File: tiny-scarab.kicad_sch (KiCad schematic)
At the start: 40 parts, among them J2 TC2050-IDC-NL, J3 CONN_PIN_HEADER_02x07, J4 CONN_PIN_HEADER_02x07, J5 3mm, J6 3mm, J7 3mm, J8 3mm

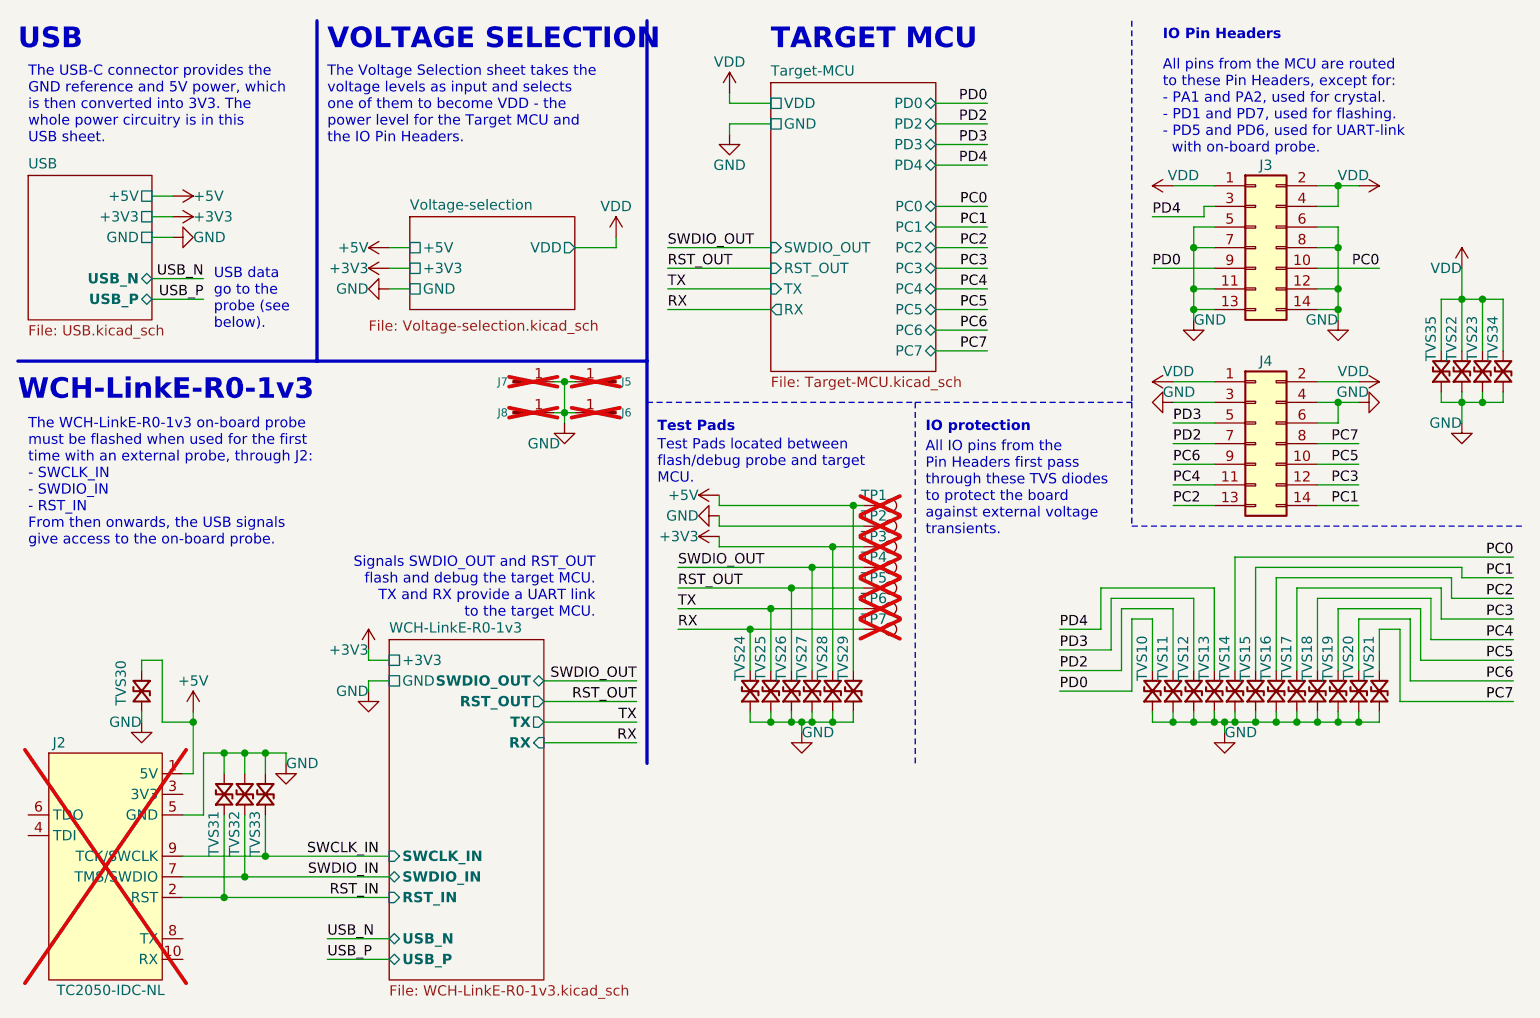
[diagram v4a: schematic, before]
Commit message: Rename net 'RST_OUT' into 'RST_CH32V003'
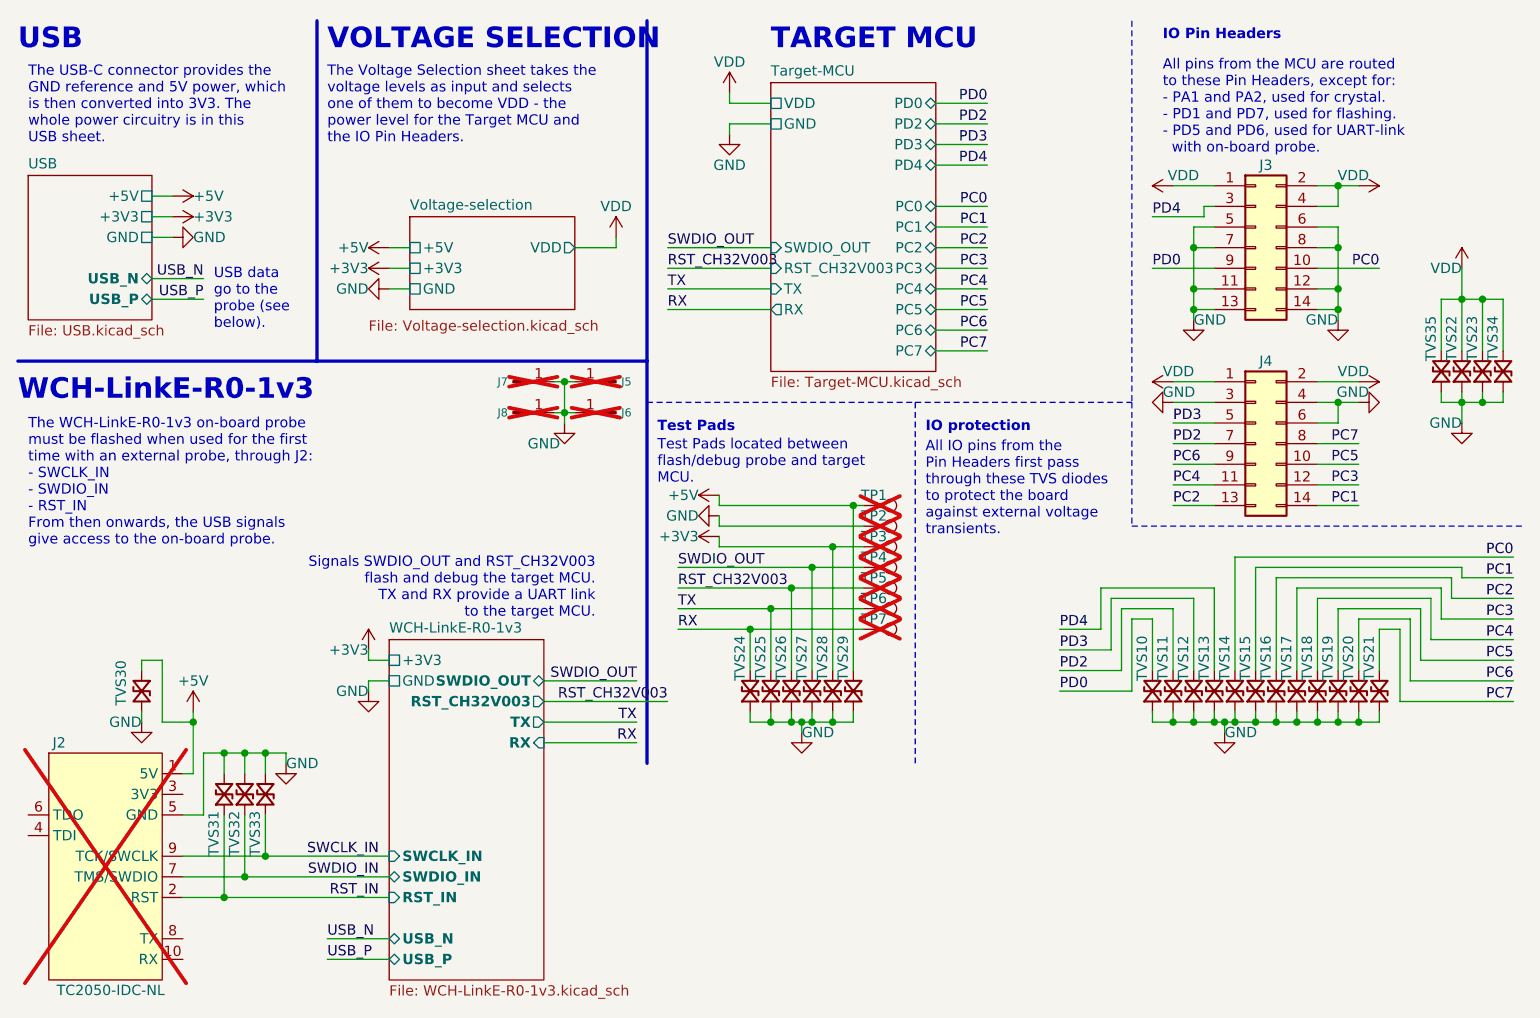
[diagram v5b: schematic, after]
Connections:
- net RST_OUT renamed RST_CH32V003
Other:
- sheet Target-MCU ports: added RST_CH32V003; removed RST_OUT
- sheet WCH-LinkE-R0-1v3 ports: added RST_CH32V003; removed RST_OUT
- note added: "Signals SWDIO_OUT and RST_CH32V003 flash and debug the target MCU. TX and RX provide a UART link to the target MCU."
- note removed: "Signals SWDIO_OUT and RST_OUT flash and debug the target MCU. TX and RX provide a UART link to the target MCU."
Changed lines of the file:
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@@
     (stroke (width 0) (type default))
   )
-  (wire (pts (xy 77.47 96.52) (xy 88.9 96.52))
+  (wire (pts (xy 77.47 96.52) (xy 92.71 96.52))
     (stroke (width 0) (type default))
   )
@@
     (effects (font (size 2.54 2.54) (thickness 0.508) bold) (justify left bottom))
   )
-  (text "Signals SWDIO_OUT and RST_OUT\nflash and debug the target MCU.\nTX and RX provide a UART link\nto the target MCU."
+  (text "Signals SWDIO_OUT and RST_CH32V003\nflash and debug the target MCU.\nTX and RX provide a UART link\nto the target MCU."
     (at 83.82 86.36 0)
     (effects (font (size 1.27 1.27)) (justify right bottom))
@@
     (effects (font (size 1.27 1.27)) (justify right bottom))
   )
-  (label "RST_OUT" (at 93.98 82.55 0) (fields_autoplaced)
+  (label "RST_CH32V003" (at 93.98 82.55 0) (fields_autoplaced)
     (effects (font (size 1.27 1.27)) (justify left bottom))
   )
@@
     (effects (font (size 1.27 1.27)) (justify left bottom))
   )
-  (label "RST_OUT" (at 92.71 43.18 0) (fields_autoplaced)
+  (label "RST_CH32V003" (at 92.71 43.18 0) (fields_autoplaced)
     (effects (font (size 1.27 1.27)) (justify left bottom))
   )
@@
     (effects (font (size 1.27 1.27)) (justify right bottom))
   )
-  (label "RST_OUT" (at 88.9 96.52 180) (fields_autoplaced)
+  (label "RST_CH32V003" (at 92.71 96.52 180) (fields_autoplaced)
     (effects (font (size 1.27 1.27)) (justify right bottom))
   )
@@
       (effects (font (size 1.27 1.27) (thickness 0.254) bold) (justify right))
     )
-    (pin "RST_OUT" output (at 77.47 96.52 0)
+    (pin "RST_CH32V003" output (at 77.47 96.52 0)
       (effects (font (size 1.27 1.27) (thickness 0.254) bold) (justify right))
     )
@@
       (effects (font (size 1.27 1.27)) (justify left))
     )
-    (pin "RST_OUT" input (at 105.41 43.18 180)
-      (effects (font (size 1.27 1.27)) (justify left))
-    )
+    (pin "RST_CH32V003" input (at 105.41 43.18 180)
+      (effects (font (size 1.27 1.27)) (justify left))
+    )

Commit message: Rename net 'RST_IN' into 'RST_CH32V305'
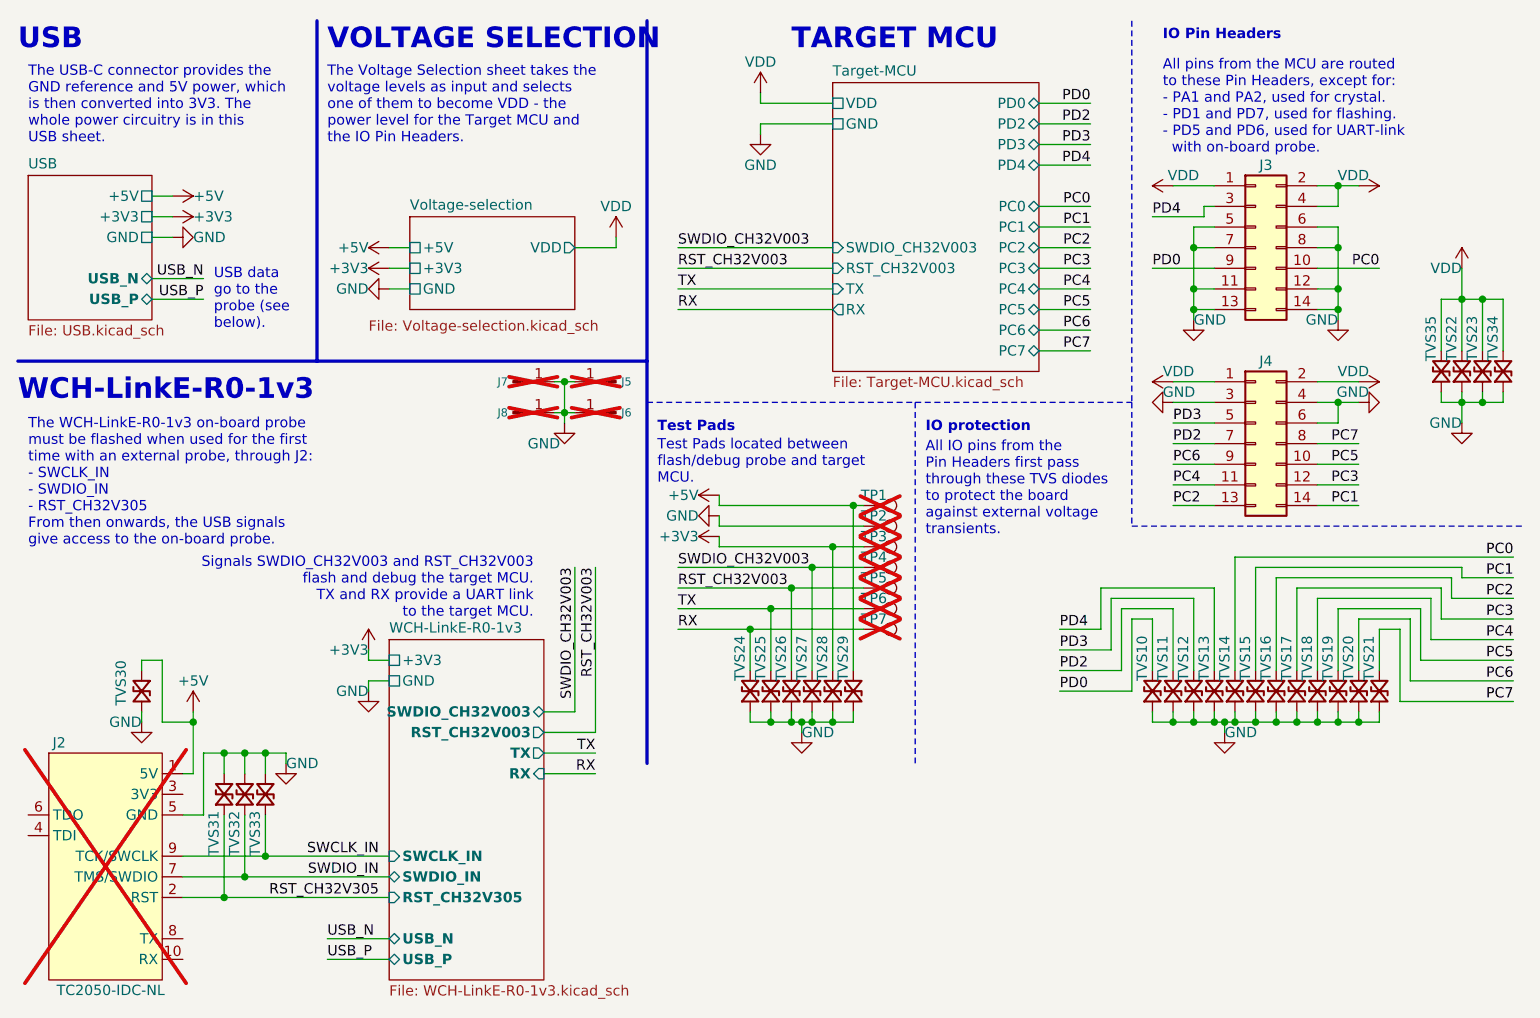
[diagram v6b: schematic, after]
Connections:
- net RST_IN renamed RST_CH32V305
- net SWDIO_OUT renamed SWDIO_CH32V003
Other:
- sheet Target-MCU ports: added SWDIO_CH32V003; removed SWDIO_OUT
- sheet WCH-LinkE-R0-1v3 ports: added RST_CH32V305, SWDIO_CH32V003; removed RST_IN, SWDIO_OUT
- note added: "Signals SWDIO_CH32V003 and RST_CH32V003 flash and debug the target MCU. TX and RX provide a UART link to the target MCU."
- note added: "The WCH-LinkE-R0-1v3 on-board probe must be flashed when used for the first time with an external probe, through J2: - SWCLK_IN - SWDIO_IN - RST_CH32V305 From then onwards, the USB signals give access to the on-board probe."
- note removed: "Signals SWDIO_OUT and RST_CH32V003 flash and debug the target MCU. TX and RX provide a UART link to the target MCU."
- note removed: "The WCH-LinkE-R0-1v3 on-board probe must be flashed when used for the first time with an external probe, through J2: - SWCLK_IN - SWDIO_IN - RST_IN From then onwards, the USB signals give access to the on-board probe."

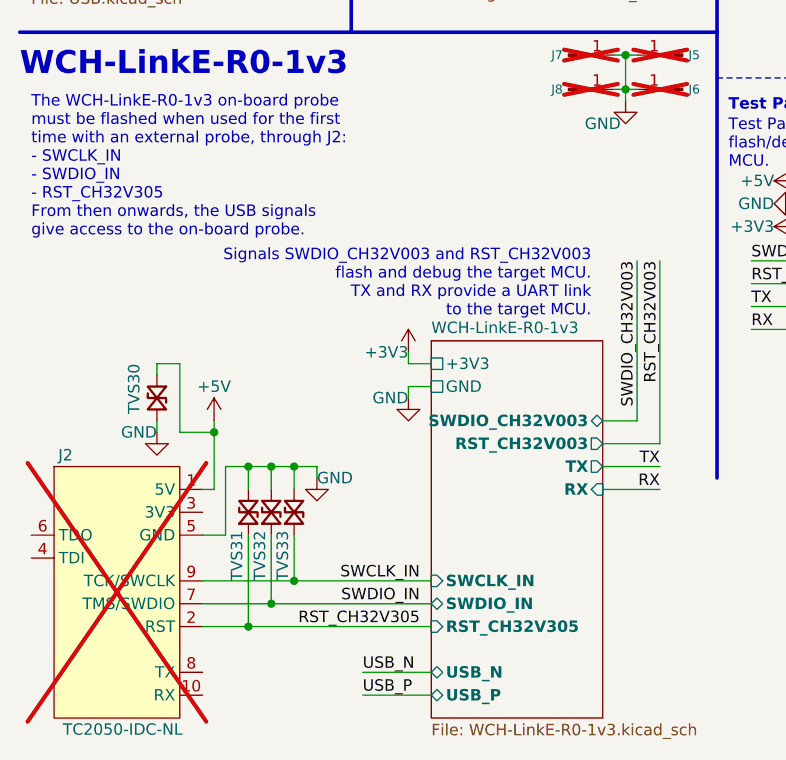
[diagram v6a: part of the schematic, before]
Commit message: Rename net 'SWDIO_IN' into 'SWDIO_CH32V305'
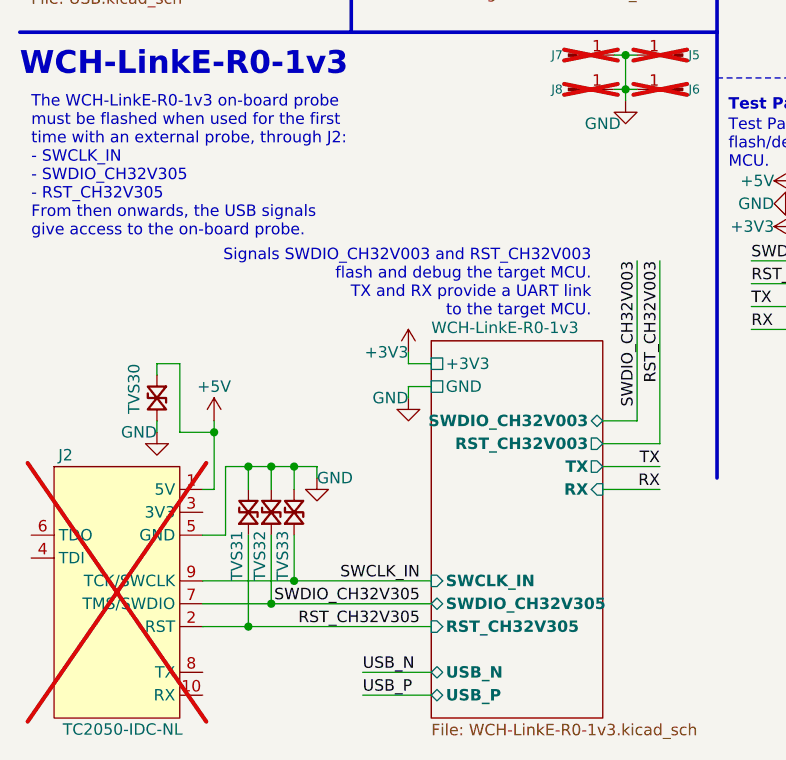
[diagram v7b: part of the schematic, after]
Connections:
- net SWDIO_IN renamed SWDIO_CH32V305
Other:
- sheet WCH-LinkE-R0-1v3 ports: added SWDIO_CH32V305; removed SWDIO_IN
- note added: "The WCH-LinkE-R0-1v3 on-board probe must be flashed when used for the first time with an external probe, through J2: - SWCLK_IN - SWDIO_CH32V305 - RST_CH32V305 From then onwards, the USB signals give access to the on-board probe."
- note removed: "The WCH-LinkE-R0-1v3 on-board probe must be flashed when used for the first time with an external probe, through J2: - SWCLK_IN - SWDIO_IN - RST_CH32V305 From then onwards, the USB signals give access to the on-board probe."
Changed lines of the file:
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@@
     (effects (font (size 2.54 2.54) (thickness 0.508) bold) (justify left bottom))
   )
-  (text "The WCH-LinkE-R0-1v3 on-board probe\nmust be flashed when used for the first\ntime with an external probe, through J2:\n- SWCLK_IN\n- SWDIO_IN\n- RST_CH32V305\nFrom then onwards, the USB signals\ngive access to the on-board probe."
+  (text "The WCH-LinkE-R0-1v3 on-board probe\nmust be flashed when used for the first\ntime with an external probe, through J2:\n- SWCLK_IN\n- SWDIO_CH32V305\n- RST_CH32V305\nFrom then onwards, the USB signals\ngive access to the on-board probe."
     (at 13.97 77.47 0)
     (effects (font (size 1.27 1.27)) (justify left bottom))
@@
     (effects (font (size 1.27 1.27)) (justify left bottom))
   )
-  (label "SWDIO_IN" (at 57.15 118.11 180) (fields_autoplaced)
+  (label "SWDIO_CH32V305" (at 57.15 118.11 180) (fields_autoplaced)
     (effects (font (size 1.27 1.27)) (justify right bottom))
   )
@@
       (effects (font (size 1.27 1.27) (thickness 0.254) bold) (justify left))
     )
-    (pin "SWDIO_IN" bidirectional (at 58.42 118.11 180)
+    (pin "SWDIO_CH32V305" bidirectional (at 58.42 118.11 180)
       (effects (font (size 1.27 1.27) (thickness 0.254) bold) (justify left))
     )

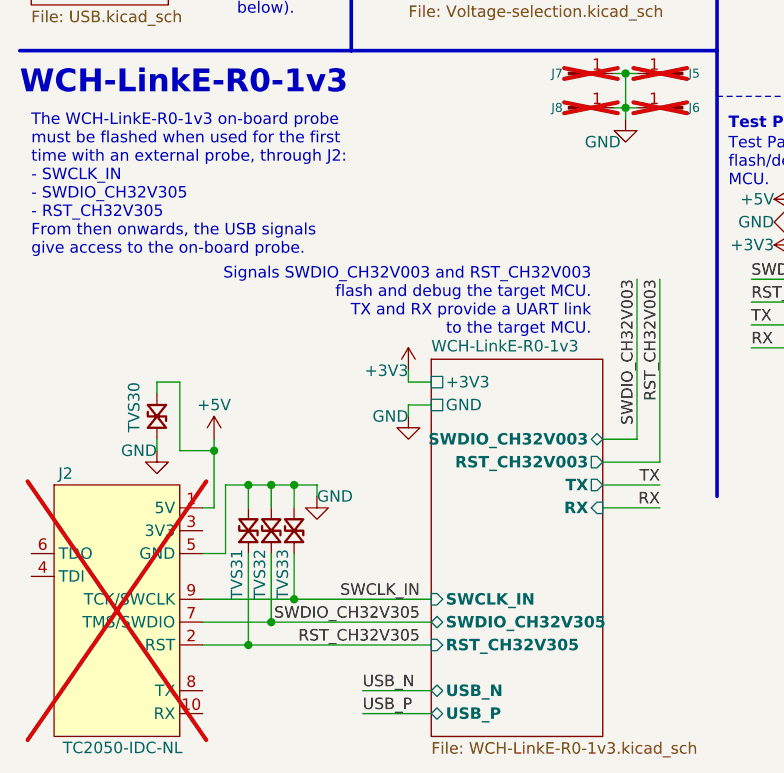
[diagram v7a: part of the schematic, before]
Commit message: Rename net 'SWCLK_IN' into 'SWCLK_CH32V305'
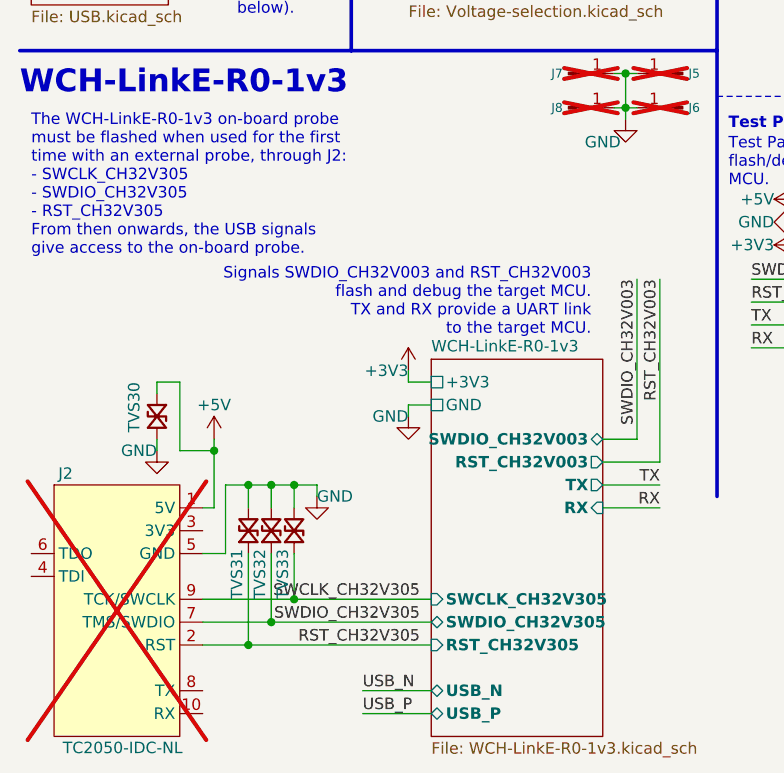
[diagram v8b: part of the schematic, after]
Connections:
- net SWCLK_IN renamed SWCLK_CH32V305
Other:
- sheet WCH-LinkE-R0-1v3 ports: added SWCLK_CH32V305; removed SWCLK_IN
- note added: "The WCH-LinkE-R0-1v3 on-board probe must be flashed when used for the first time with an external probe, through J2: - SWCLK_CH32V305 - SWDIO_CH32V305 - RST_CH32V305 From then onwards, the USB signals give access to the on-board probe."
- note removed: "The WCH-LinkE-R0-1v3 on-board probe must be flashed when used for the first time with an external probe, through J2: - SWCLK_IN - SWDIO_CH32V305 - RST_CH32V305 From then onwards, the USB signals give access to the on-board probe."
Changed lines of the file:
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@@
     (effects (font (size 2.54 2.54) (thickness 0.508) bold) (justify left bottom))
   )
-  (text "The WCH-LinkE-R0-1v3 on-board probe\nmust be flashed when used for the first\ntime with an external probe, through J2:\n- SWCLK_IN\n- SWDIO_CH32V305\n- RST_CH32V305\nFrom then onwards, the USB signals\ngive access to the on-board probe."
+  (text "The WCH-LinkE-R0-1v3 on-board probe\nmust be flashed when used for the first\ntime with an external probe, through J2:\n- SWCLK_CH32V305\n- SWDIO_CH32V305\n- RST_CH32V305\nFrom then onwards, the USB signals\ngive access to the on-board probe."
     (at 13.97 77.47 0)
     (effects (font (size 1.27 1.27)) (justify left bottom))
@@
     (effects (font (size 1.27 1.27)) (justify left bottom))
   )
-  (label "SWCLK_IN" (at 57.15 115.57 180) (fields_autoplaced)
+  (label "SWCLK_CH32V305" (at 57.15 115.57 180) (fields_autoplaced)
     (effects (font (size 1.27 1.27)) (justify right bottom))
   )
@@
       (effects (font (size 1.27 1.27)) (justify left top))
     )
-    (pin "SWCLK_IN" input (at 58.42 115.57 180)
+    (pin "SWCLK_CH32V305" input (at 58.42 115.57 180)
       (effects (font (size 1.27 1.27) (thickness 0.254) bold) (justify left))
     )
